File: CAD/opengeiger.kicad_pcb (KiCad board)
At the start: 2 copper layers, 116 x 31 mm, 92 parts, among them J1 Conn_01x04, J10 Conn_01x04, J3 Conn_01x06, J5 Conn_01x04, J8 USB_C_Receptacle_USB2.0, Q1 STN0214, Q2 PMBT2222A,215, Q3 DMG2302UK-7, Q4 UMH3N, SW1 TL3301NF160QG/TR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

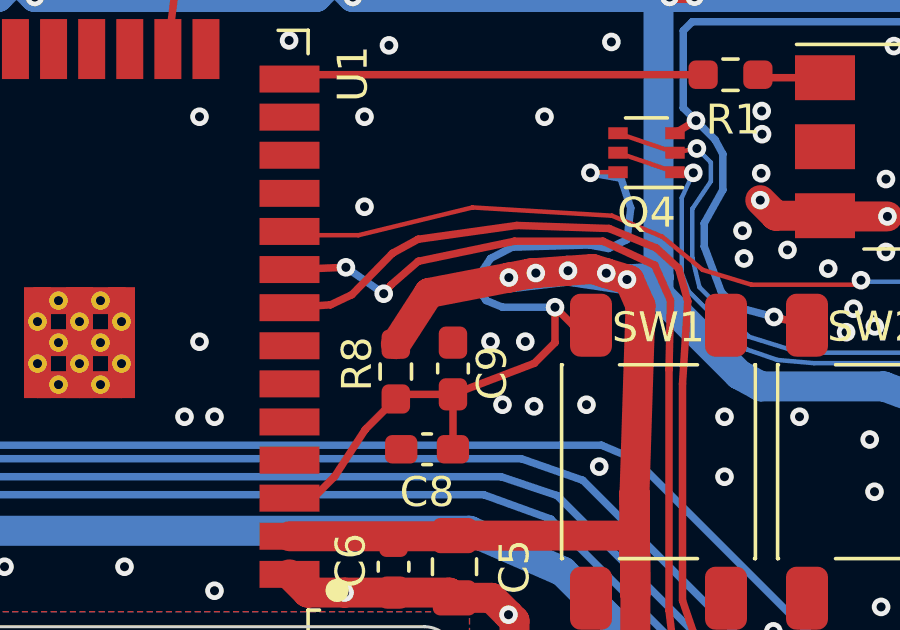
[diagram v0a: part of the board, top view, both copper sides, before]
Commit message: Feat: Fixed adc port and captive portal
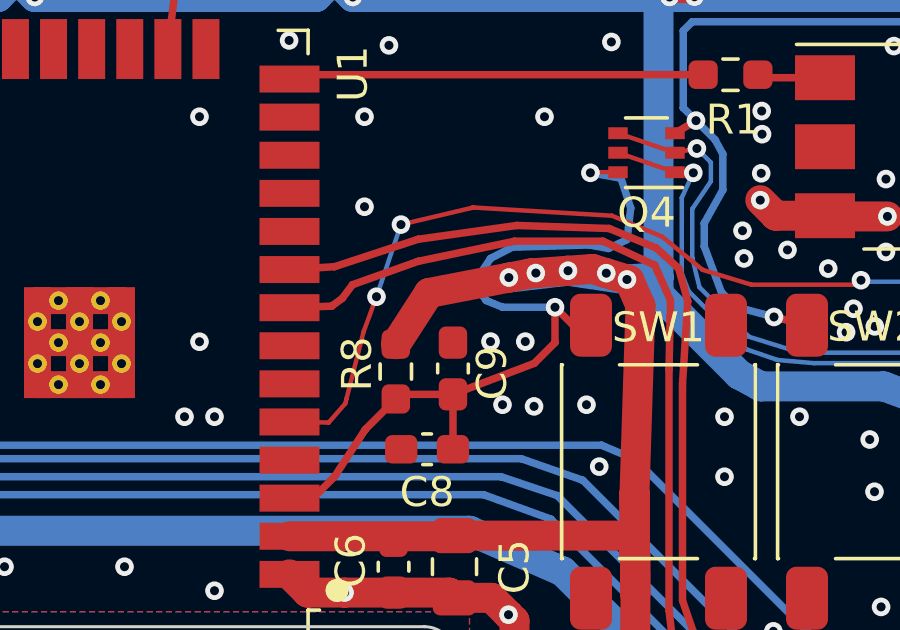
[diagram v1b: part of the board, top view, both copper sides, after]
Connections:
- U1 pad 10: RFB -> unconnected-(U1-Pad10)
- U1 pad 5: unconnected-(U1-Pad5) -> RFB
- U1 pad 8: CLICKER -> GPIO32
- U1 pad 9: GPIO32 -> CLICKER
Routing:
- net RFB: track 88.8 -> 93.4 mm, vias 2 -> 4
- net CLICKER: track 67.7 -> 67.1 mm
- net GPIO32: track 63.1 -> 62.8 mm, vias 2 -> 0

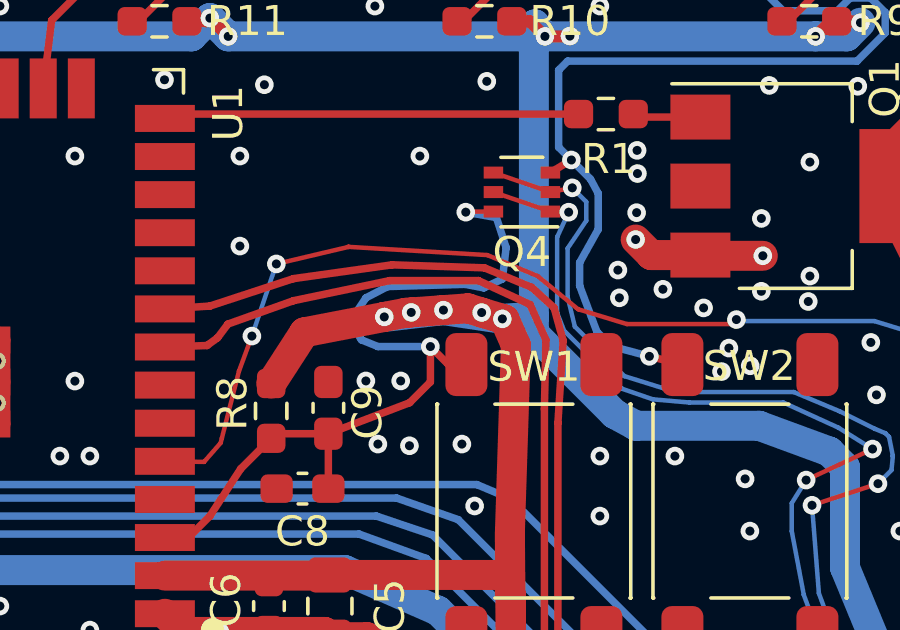
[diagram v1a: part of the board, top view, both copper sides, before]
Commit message: Feat: New order from jlcpcb rev 0.2.1
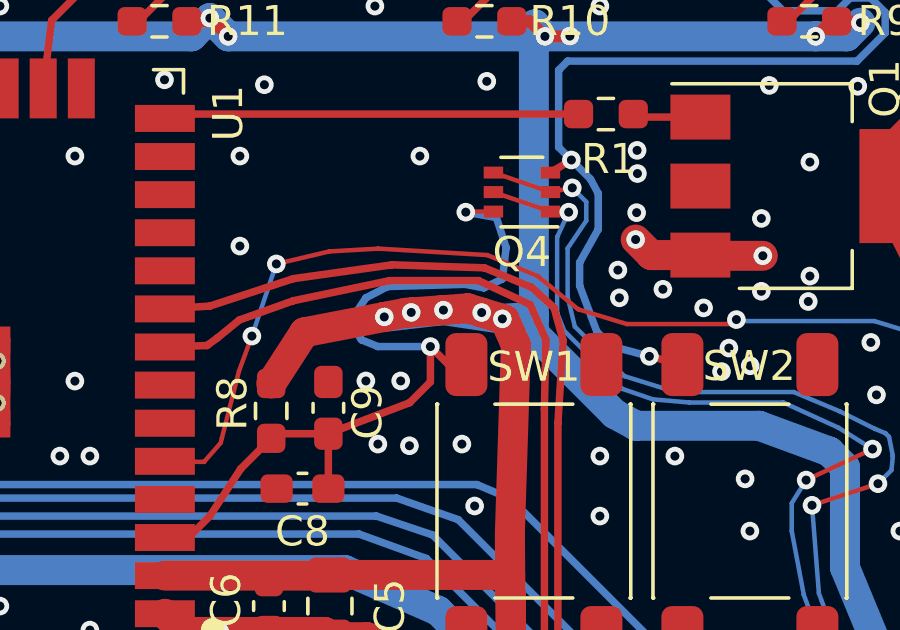
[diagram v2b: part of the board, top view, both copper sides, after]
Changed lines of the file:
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@@
   (segment (start 112.85 77.6) (end 114.522896 77.977104) (width 0.25) (layer "F.Cu") (net 8))
   (segment (start 115.165 79.215) (end 115.9975 79.215) (width 0.25) (layer "F.Cu") (net 8))
-  (segment (start 112.495 92.52) (end 112.75 92.52) (width 0.25) (layer "F.Cu") (net 8))
   (segment (start 79.422 81.422) (end 78.5 83.745) (width 0.25) (layer "F.Cu") (net 8))
   (segment (start 108.35 85.55) (end 109.05 85.13) (width 0.25) (layer "F.Cu") (net 8))
@@
   (segment (start 74.256875 79) (end 72.75 80.506875) (width 0.25) (layer "F.Cu") (net 17))
   (segment (start 97.4 94.4) (end 97.36 94.56) (width 0.15) (layer "F.Cu") (net 18))
-  (segment (start 101.6 88.025) (end 101.626571 88.026571) (width 0.15) (layer "F.Cu") (net 18))
-  (segment (start 101.626571 88.026571) (end 106.25 88.3) (width 0.15) (layer "F.Cu") (net 18))
+  (segment (start 102.613753 88.084953) (end 106.25 88.3) (width 0.15) (layer "F.Cu") (net 18))
   (segment (start 97.969231 92.169231) (end 97.4 94.4) (width 0.15) (layer "F.Cu") (net 18))
   (segment (start 98.4 91) (end 97.969231 92.169231) (width 0.15) (layer "F.Cu") (net 18))
@@
   (segment (start 109.270775 90.104225) (end 110.9 90.6) (width 0.15) (layer "F.Cu") (net 18))
   (segment (start 167.75 78.95) (end 169.05 78.95) (width 0.4) (layer "F.Cu") (net 18))
-  (segment (start 99.215409 88.595624) (end 101.626571 88.026571) (width 0.15) (layer "F.Cu") (net 18))
+  (segment (start 99.215409 88.595624) (end 100.98062 88.17902) (width 0.15) (layer "F.Cu") (net 18))
   (segment (start 96.805797 95.194203) (end 97.36 94.56) (width 0.15) (layer "F.Cu") (net 18))
   (segment (start 96.805797 95.194203) (end 95.5 95.175) (width 0.15) (layer "F.Cu") (net 18))
+  (segment (start 100.98062 88.17902) (end 102.613753 88.084953) (width 0.15) (layer "F.Cu") (net 18))
   (segment (start 107.925 89) (end 109.270775 90.104225) (width 0.15) (layer "F.Cu") (net 18))
   (segment (start 170.5 79.0875) (end 170.3625 78.95) (width 0.4) (layer "F.Cu") (net 18))
@@
   (segment (start 76.612966 84.737034) (end 77.325 85.925) (width 0.25) (layer "F.Cu") (net 38))
   (segment (start 133.206699 96.706699) (end 133.91654 96.33346) (width 0.25) (layer "F.Cu") (net 43))
-  (segment (start 99.79 89.82) (end 97.6 90.6) (width 0.25) (layer "F.Cu") (net 43))
   (segment (start 115.136443 103.363557) (end 110.313557 103.363557) (width 0.25) (layer "F.Cu") (net 43))
   (segment (start 135.426906 96.823094) (end 139 100.18) (width 0.25) (layer "F.Cu") (net 43))
+  (segment (start 99.79 89.82) (end 97.982255 90.463855) (width 0.25) (layer "F.Cu") (net 43))
   (segment (start 107.675 89.95) (end 108.2 91.125) (width 0.25) (layer "F.Cu") (net 43))
   (segment (start 130.393886 100.443886) (end 132.281699 97.631699) (width 0.25) (layer "F.Cu") (net 43))
@@
   (segment (start 133.206699 96.706699) (end 132.281699 97.631699) (width 0.25) (layer "F.Cu") (net 43))
   (segment (start 103 89.15) (end 105.95 89.15) (width 0.25) (layer "F.Cu") (net 43))
-  (segment (start 97.6 90.6) (end 97.257143 91.057143) (width 0.25) (layer "F.Cu") (net 43))
   (segment (start 108.15 101.45) (end 108.325 102.95) (width 0.25) (layer "F.Cu") (net 43))
   (segment (start 130.074039 101.549039) (end 130.393886 100.443886) (width 0.25) (layer "F.Cu") (net 43))
   (segment (start 108.325 102.95) (end 109.1 103.4) (width 0.25) (layer "F.Cu") (net 43))
+  (segment (start 97.982255 90.463855) (end 97.257143 91.057143) (width 0.25) (layer "F.Cu") (net 43))
   (segment (start 117.392211 103.857789) (end 118.375482 104.624518) (width 0.25) (layer "F.Cu") (net 43))
   (segment (start 122.9 105.1) (end 120.875 105.1) (width 0.25) (layer "F.Cu") (net 43))

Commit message: Feat: Added LCSC part numbers to schematics
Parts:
- D14, D2, D3, D4, D5, D6, D7: value 0603RBD0700S01 -> RED_LED

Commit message: Feat: Update to 0.2.2
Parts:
- added F1: 6.35mm Fuse holder, eikgeiger:FC-102-22, B.Cu at (70.7, 87.6)
- added F2: 6.35mm Fuse holder, eikgeiger:FC-102-22, B.Cu at (175.3, 87.6)
- added kibuzzard-6571CD20: G***, kibuzzard-6571CD20, B.Cu at (162.9, 87.7)
- added kibuzzard-6571CD43: G***, kibuzzard-6571CD43, B.Cu at (84.9, 87.7)
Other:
- board text added: "V 0.2.2"
- board text removed: "V 0.2.1"
